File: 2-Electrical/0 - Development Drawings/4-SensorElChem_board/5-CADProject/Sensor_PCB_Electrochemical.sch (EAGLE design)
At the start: 21 parts, among them IC4 LMP91000SD_NOPB, IC5 REF3125AQDBZRQ1, J10 2wire, Q1 PMBFJ177,215, X1 3-ELECTRODE-GAS-SENSOR_SOCKET

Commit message: programing procedure, elchem board
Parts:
- removed FID1, FID2, FID4: FIDUCIAL"", microbuilder:FIDUCIAL""
- added C1: DNI, resistor:C-EUC0603K
- added FID3, FID5, FID6, FID7, FID8, FID9: FIDUCIAL1X1UNMASKED, microbuilder:FIDUCIAL1X1UNMASKED
- added JP2: JUMPER-SMT_3_NO_NO_SILK, SparkFun-Jumpers:JUMPER-SMT_3_NO_NO_SILK
- C12, C2, C8, C9: PARTNO (none) -> GRM188R71C104KA01D
- IC4: PARTNO (none) -> LMP91000
- IC5: PARTNO (none) -> REF3125AQDBZRQ1
- J1: PARTNO (none) -> 30306-6002HB
- LED1: PARTNO (none) -> IN-S63AT5G
- Q1: PARTNO (none) -> PMBFJ177,215
- R12: PARTNO (none) -> CRCW060310R0FKEA
- R20, R21: PARTNO (none) -> CRCW060310K0FKEA
- R22: PARTNO (none) -> CRCW06030000Z0EA
- R24: PARTNO (none) -> CRCW0603100RFKEA
- U2, X1: PARTNO (none) -> INSTALLED_BY_CUSTOMER
- renumbered J10 to J2, U$1 to J1, U$2 to U2
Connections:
- removed net N$19: R22.2, U2.CE
- new net CE_CO: JP2.1, R22.2, U2.CE
- new net N$2: C1.1, IC4.C1
- new net N$4: C1.2, IC4.C2
- net CE: now also JP2.2
- net RE: now also JP2.3

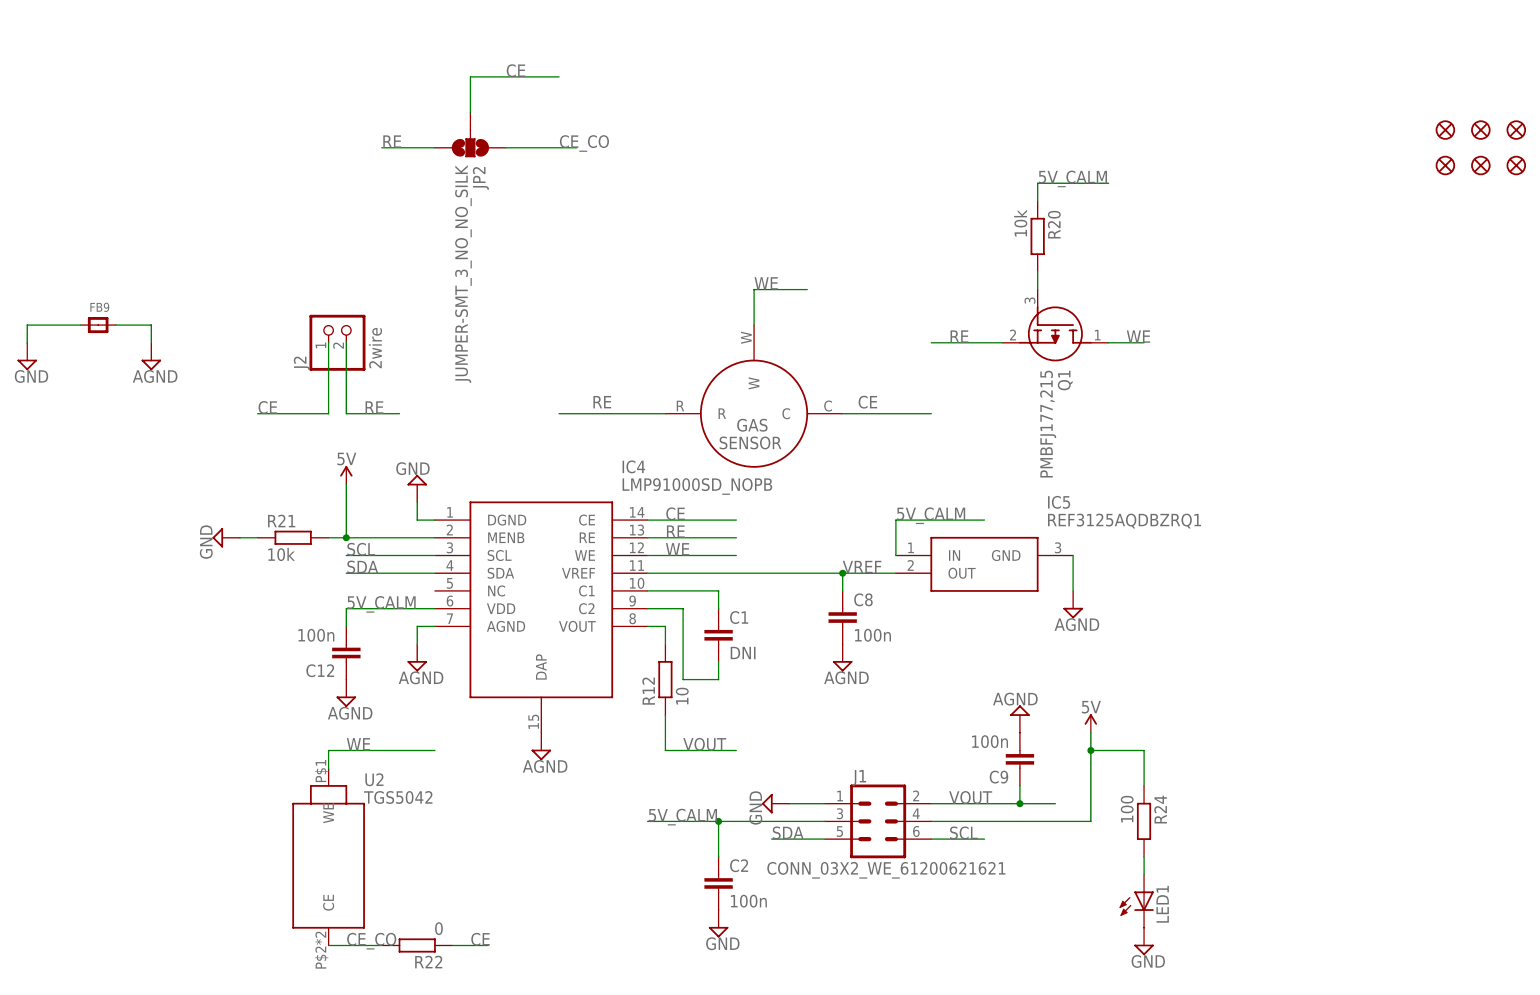
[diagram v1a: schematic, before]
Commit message: data processing, orders review, tests, elchem pcb RE CE swap
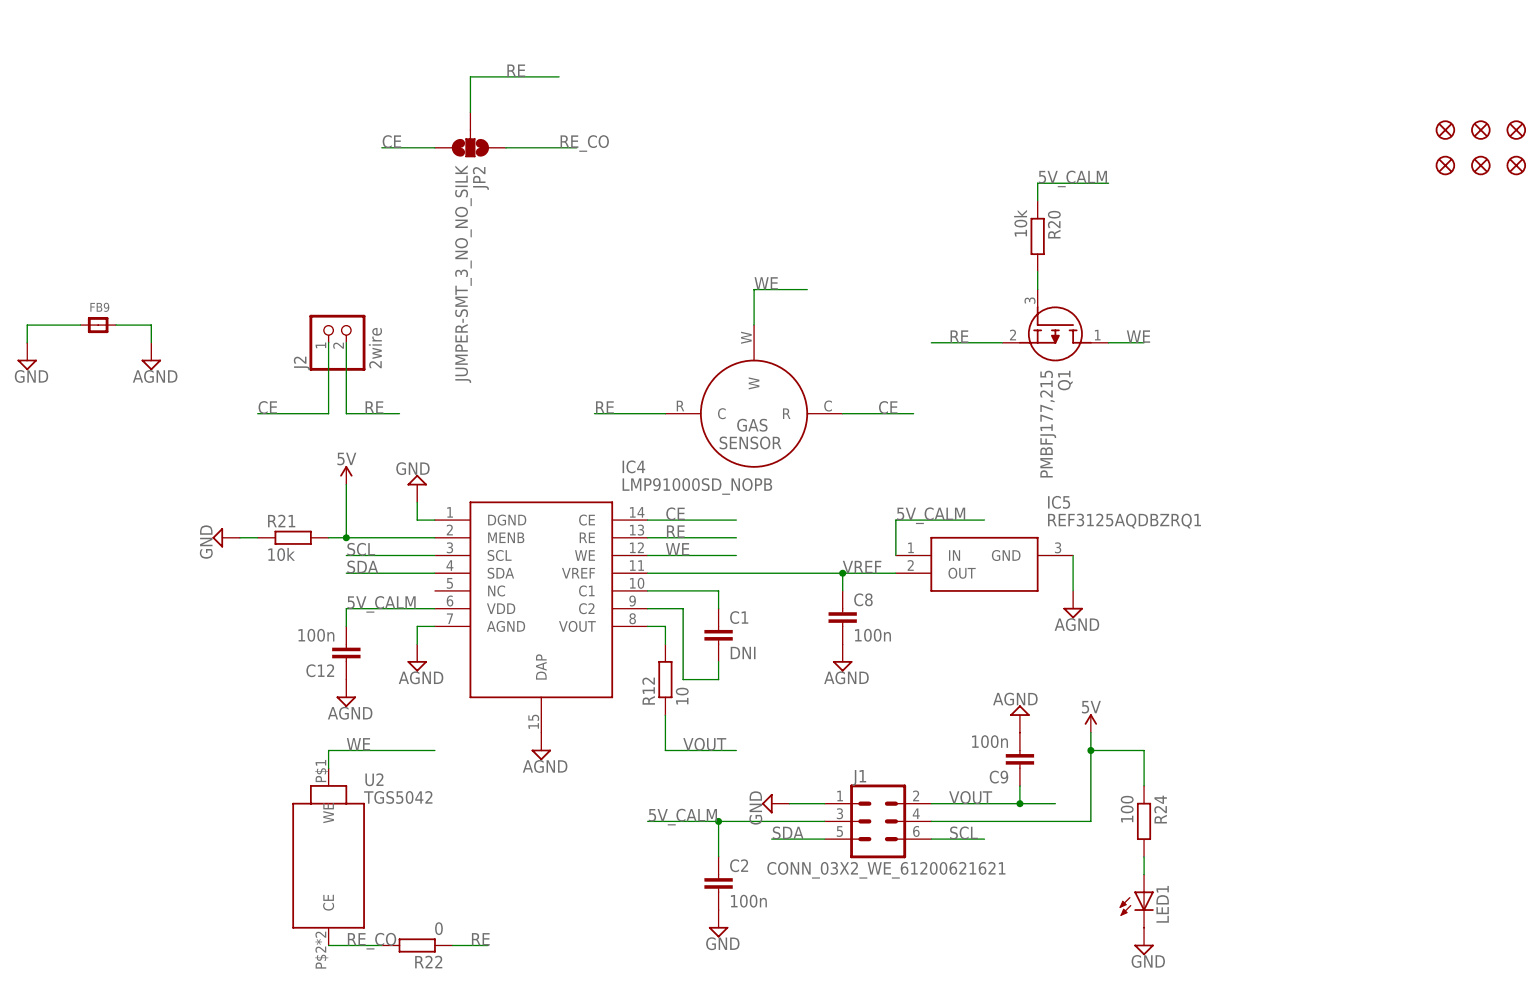
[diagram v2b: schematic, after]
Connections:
- net CE_CO renamed RE_CO
- net CE: now also JP2.3, X1.R; no longer JP2.2, R22.1, X1.C
- net RE: now also JP2.2, R22.1, X1.C; no longer JP2.3, X1.R
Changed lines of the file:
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@@
 <attributes>
 <attribute name="CNAME" value="Electrochemical gas sensor PCB"/>
-<attribute name="CREVISION" value="01"/>
+<attribute name="CREVISION" value="02"/>
 </attributes>
 <variantdefs>
@@
 <net name="RE" class="0">
 <segment>
-<pinref part="X1" gate="G$1" pin="R"/>
-<wire x1="129.54" y1="116.84" x2="144.78" y2="116.84" width="0.1524" layer="91"/>
-<label x="137.16" y="119.38" size="1.778" layer="95" rot="R180"/>
-</segment>
-<segment>
 <pinref part="IC4" gate="G$1" pin="RE"/>
 <wire x1="142.24" y1="99.06" x2="154.94" y2="99.06" width="0.1524" layer="91"/>
@@
 </segment>
 <segment>
-<wire x1="111.76" y1="154.94" x2="104.14" y2="154.94" width="0.1524" layer="91"/>
-<label x="104.14" y="154.94" size="1.778" layer="95"/>
-<pinref part="JP2" gate="G$1" pin="3"/>
+<pinref part="R22" gate="G$1" pin="1"/>
+<wire x1="114.3" y1="40.64" x2="119.38" y2="40.64" width="0.1524" layer="91"/>
+<label x="116.84" y="40.64" size="1.778" layer="95"/>
+</segment>
+<segment>
+<pinref part="JP2" gate="G$1" pin="2"/>
+<wire x1="116.84" y1="160.02" x2="116.84" y2="165.1" width="0.1524" layer="91"/>
+<wire x1="116.84" y1="165.1" x2="129.54" y2="165.1" width="0.1524" layer="91"/>
+<label x="121.92" y="165.1" size="1.778" layer="95"/>
+</segment>
+<segment>
+<pinref part="X1" gate="G$1" pin="C"/>
+<wire x1="144.78" y1="116.84" x2="134.62" y2="116.84" width="0.1524" layer="91"/>
+<label x="134.62" y="116.84" size="1.778" layer="95"/>
 </segment>
 </net>
 <net name="CE" class="0">
-<segment>
-<pinref part="X1" gate="G$1" pin="C"/>
-<wire x1="182.88" y1="116.84" x2="170.18" y2="116.84" width="0.1524" layer="91"/>
-<label x="175.26" y="119.38" size="1.778" layer="95" rot="R180"/>
-</segment>
 <segment>
 <pinref part="IC4" gate="G$1" pin="CE"/>
@@
 </segment>
 <segment>
-<pinref part="R22" gate="G$1" pin="1"/>
-<wire x1="114.3" y1="40.64" x2="119.38" y2="40.64" width="0.1524" layer="91"/>
-<label x="116.84" y="40.64" size="1.778" layer="95"/>
-</segment>
-<segment>
-<pinref part="JP2" gate="G$1" pin="2"/>
-<wire x1="116.84" y1="160.02" x2="116.84" y2="165.1" width="0.1524" layer="91"/>
-<wire x1="116.84" y1="165.1" x2="129.54" y2="165.1" width="0.1524" layer="91"/>
-<label x="121.92" y="165.1" size="1.778" layer="95"/>
+<wire x1="111.76" y1="154.94" x2="104.14" y2="154.94" width="0.1524" layer="91"/>
+<label x="104.14" y="154.94" size="1.778" layer="95"/>
+<pinref part="JP2" gate="G$1" pin="3"/>
+</segment>
+<segment>
+<pinref part="X1" gate="G$1" pin="R"/>
+<wire x1="170.18" y1="116.84" x2="180.34" y2="116.84" width="0.1524" layer="91"/>
+<label x="175.26" y="116.84" size="1.778" layer="95"/>
 </segment>
 </net>
@@
 </segment>
 </net>
-<net name="CE_CO" class="0">
-<segment>
-<pinref part="R22" gate="G$1" pin="2"/>
-<pinref part="U2" gate="G$1" pin="CE"/>
-<wire x1="104.14" y1="40.64" x2="96.52" y2="40.64" width="0.1524" layer="91"/>
-<label x="99.06" y="40.64" size="1.778" layer="95"/>
-</segment>
-<segment>
-<pinref part="JP2" gate="G$1" pin="1"/>
-<wire x1="121.92" y1="154.94" x2="132.08" y2="154.94" width="0.1524" layer="91"/>
-<label x="129.54" y="154.94" size="1.778" layer="95"/>
-</segment>
-</net>
 <net name="N$1" class="0">
 <segment>
@@
 </segment>
 </net>
+<net name="RE_CO" class="0">
+<segment>
+<pinref part="JP2" gate="G$1" pin="1"/>
+<wire x1="121.92" y1="154.94" x2="132.08" y2="154.94" width="0.1524" layer="91"/>
+<label x="129.54" y="154.94" size="1.778" layer="95"/>
+</segment>
+<segment>
+<pinref part="R22" gate="G$1" pin="2"/>
+<pinref part="U2" gate="G$1" pin="CE"/>
+<wire x1="104.14" y1="40.64" x2="96.52" y2="40.64" width="0.1524" layer="91"/>
+<label x="99.06" y="40.64" size="1.778" layer="95"/>
+</segment>
+</net>
